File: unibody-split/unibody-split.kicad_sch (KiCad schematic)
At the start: 94 parts, among them IC1 AP130-20, SW1 SW_Push, SW10 SW_Push, SW11 SW_Push, SW12 SW_Push, SW13 SW_Push, SW14 SW_Push, SW15 SW_Push, SW16 SW_Push, SW17 SW_Push, SW18 SW_Push, SW19 SW_Push, SW2 SW_Push, SW20 SW_Push, SW21 SW_Push, SW22 SW_Push, SW23 SW_Push, SW24 SW_Push, SW25 SW_Push, SW26 SW_Push, SW27 SW_Push, SW28 SW_Push, SW29 SW_Push, SW3 SW_Push, SW30 SW_Push, SW31 SW_Push, SW32 SW_Push, SW33 SW_Push, SW34 SW_Push, SW35 SW_Push, SW36 SW_Push, SW37 SW_Push, SW38 SW_Push, SW39 SW_Push, SW4 SW_Push, SW40 SW_Push, SW41 SW_Push, SW42 SW_Push, SW5 SW_Push, SW6 SW_Push, SW7 SW_Push, SW8 SW_Push, SW9 SW_Push, U1 Pico, U2 PMW3360DM-T2QU, U3 HackPackv4-rescue:PSP_1000_JS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

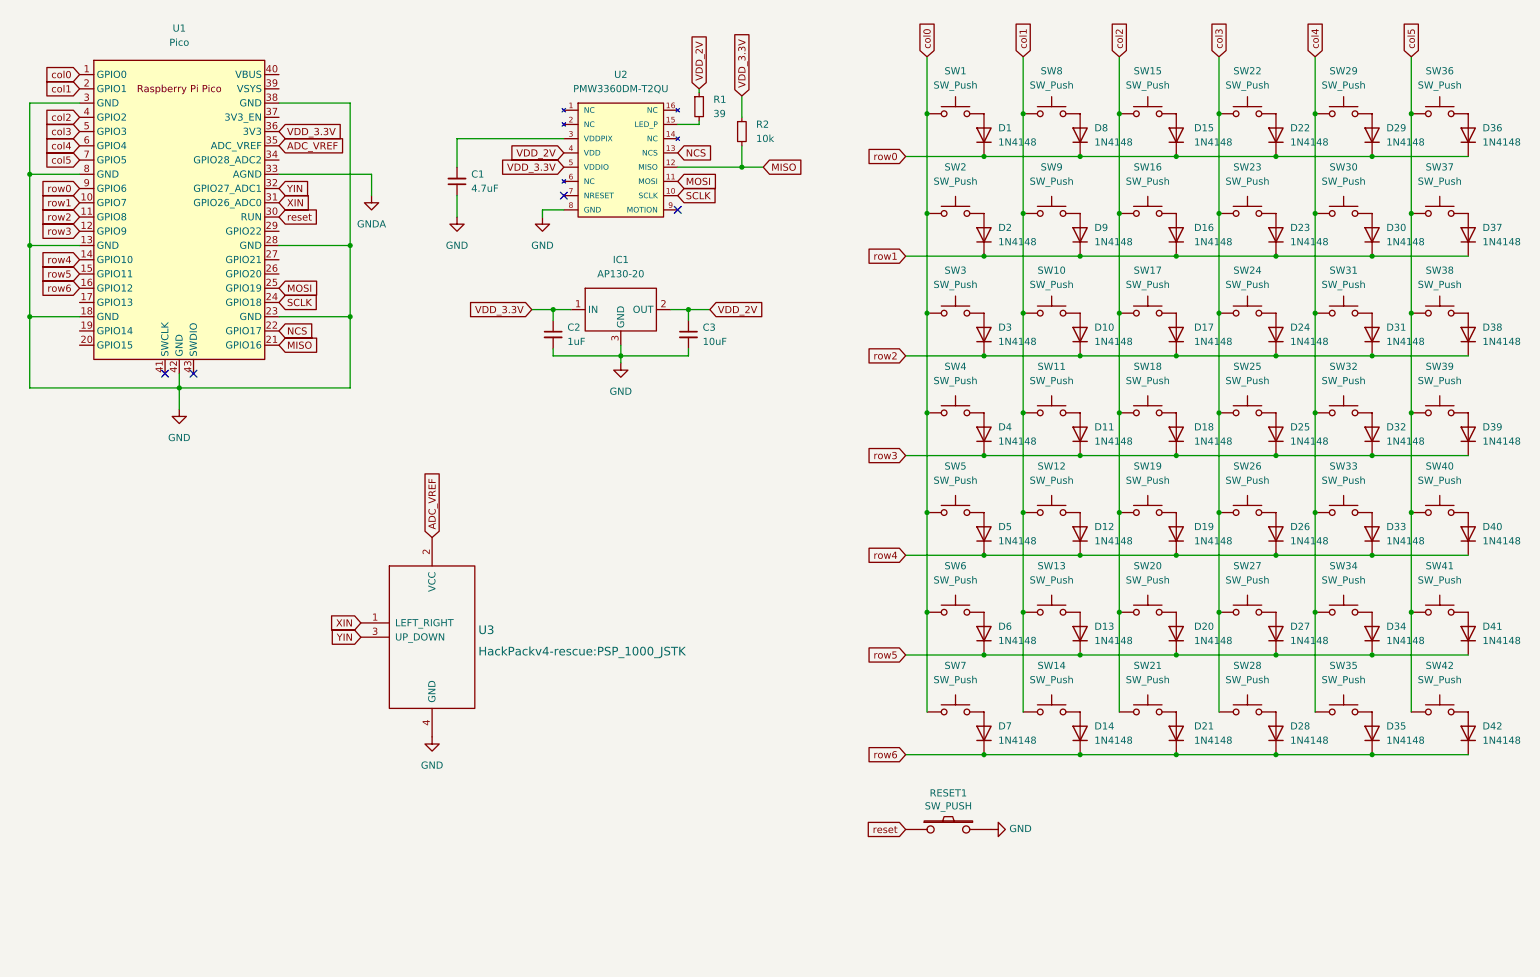
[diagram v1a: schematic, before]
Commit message: Add OLED to schematics
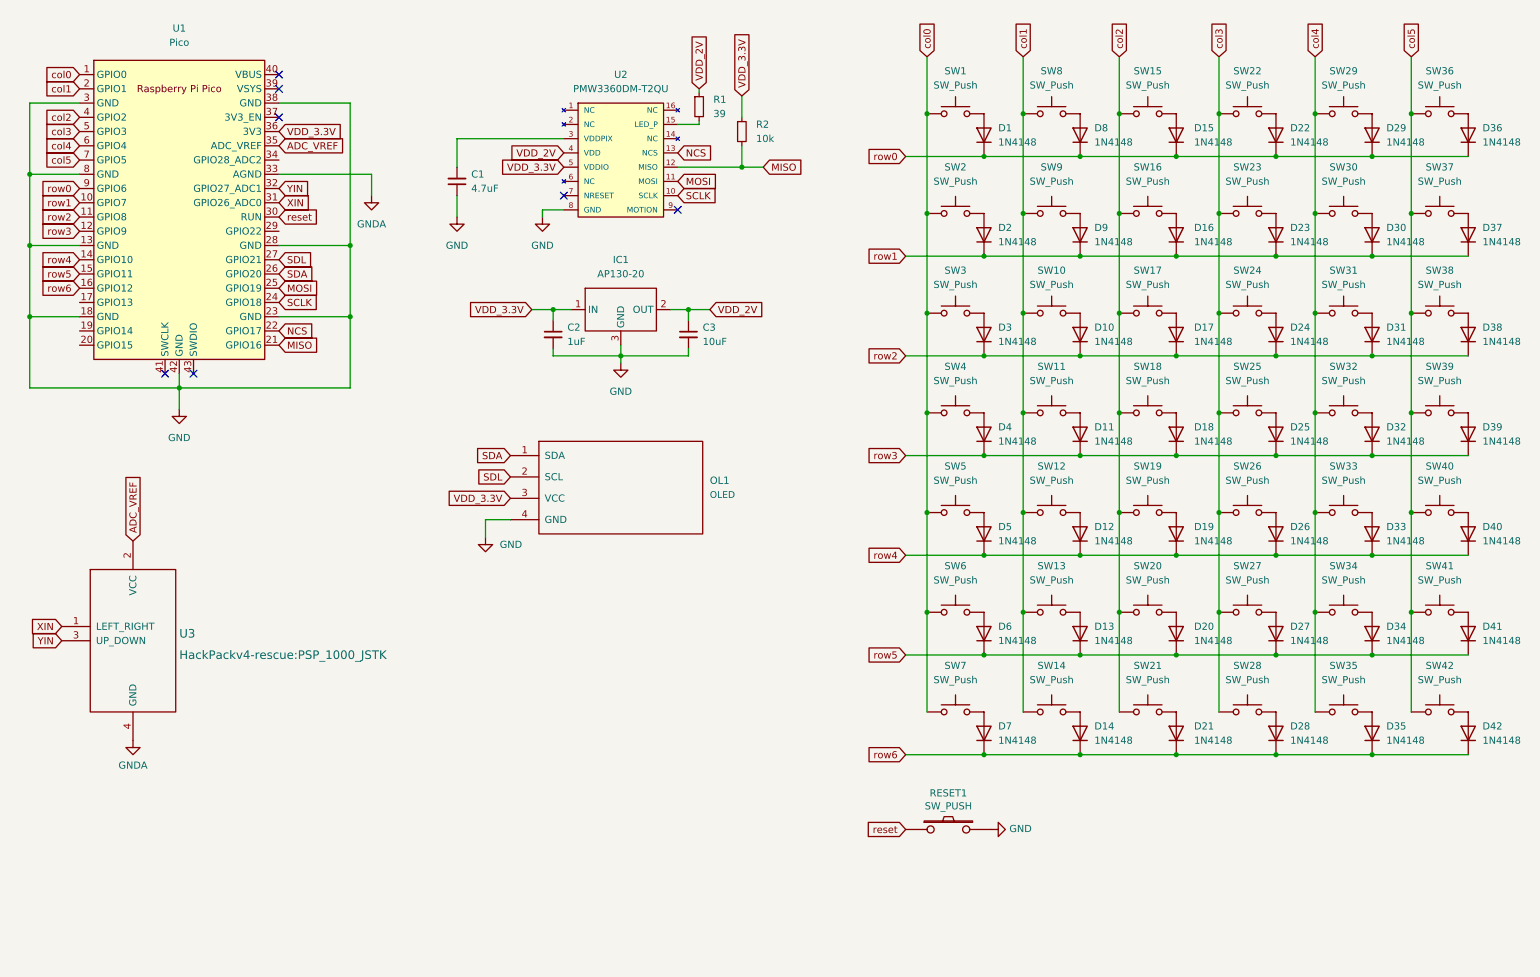
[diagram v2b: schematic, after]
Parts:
- added OL1: OLED, kbd:OLED_v2, symbol kbd:OLED
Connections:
- net GND: now also OL1.4 (GND); no longer U3.4 (GND)
- net GNDA: now also U3.4 (GND)
- net VDD_3.3V: now also OL1.3 (VCC)
- net SDA: now reaches U1.26 (GPIO20)
- net SDA: now also OL1.1 (SDA)
- net SDL: now reaches U1.27 (GPIO21)
- net SDL: now also OL1.2 (SCL)
- no-connect marks 4 -> 7
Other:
- moved on the sheet: U3
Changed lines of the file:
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@@
   (no_connect (at 111.76 45.72))
   (no_connect (at 132.08 48.26))
+  (no_connect (at 60.96 26.67))
+  (no_connect (at 60.96 31.75))
+  (no_connect (at 60.96 24.13))
   (no_connect (at 45.72 77.47))
   (no_connect (at 40.64 77.47))
@@
     (stroke (width 0) (type default) (color 0 0 0 0))
   )
+  (wire (pts (xy 102.235 103.505) (xy 97.79 103.505))
+    (stroke (width 0) (type default) (color 0 0 0 0))
+  )
   (wire (pts (xy 228.6 102.235) (xy 228.6 120.015))
     (stroke (width 0) (type default) (color 0 0 0 0))
@@
   )
   (wire (pts (xy 245.745 120.015) (xy 245.745 137.795))
+    (stroke (width 0) (type default) (color 0 0 0 0))
+  )
+  (wire (pts (xy 97.79 103.505) (xy 97.79 106.68))
     (stroke (width 0) (type default) (color 0 0 0 0))
   )
@@
     )
   )
+  (global_label "SDL" (shape input) (at 102.235 95.885 180) (fields_autoplaced)
+    (effects (font (size 1.27 1.27)) (justify right))
+    (property "Intersheet References" "${INTERSHEET_REFS}" (id 0) (at 96.3143 95.9644 0)
+      (effects (font (size 1.27 1.27)) (justify right) hide)
+    )
+  )
   (global_label "VDD_2V" (shape input) (at 135.89 26.67 90) (fields_autoplaced)
     (effects (font (size 1.27 1.27)) (justify left))
@@
     )
   )
+  (global_label "SDA" (shape input) (at 102.235 92.075 180) (fields_autoplaced)
+    (effects (font (size 1.27 1.27)) (justify right))
+    (property "Intersheet References" "${INTERSHEET_REFS}" (id 0) (at 96.2538 92.1544 0)
+      (effects (font (size 1.27 1.27)) (justify right) hide)
+    )
+  )
   (global_label "MOSI" (shape input) (at 132.08 43.18 0) (fields_autoplaced)
     (effects (font (size 1.27 1.27)) (justify left))
@@
     )
   )
+  (global_label "SDA" (shape input) (at 60.96 59.69 0) (fields_autoplaced)
+    (effects (font (size 1.27 1.27)) (justify left))
+    (property "Intersheet References" "${INTERSHEET_REFS}" (id 0) (at 66.9412 59.6106 0)
+      (effects (font (size 1.27 1.27)) (justify left) hide)
+    )
+  )
   (global_label "reset" (shape input) (at 172.72 158.75 180) (fields_autoplaced)
     (effects (font (size 1.27 1.27)) (justify right))
@@
     )
   )
-  (global_label "XIN" (shape input) (at 75.565 121.92 180) (fields_autoplaced)
-    (effects (font (size 1.27 1.27)) (justify right))
-    (property "Intersheet References" "${INTERSHEET_REFS}" (id 0) (at 70.0071 121.8406 0)
+  (global_label "XIN" (shape input) (at 22.225 122.555 180) (fields_autoplaced)
+    (effects (font (size 1.27 1.27)) (justify right))
+    (property "Intersheet References" "${INTERSHEET_REFS}" (id 0) (at 16.6671 122.4756 0)
       (effects (font (size 1.27 1.27)) (justify right) hide)
     )
@@
     )
   )
+  (global_label "VDD_3.3V" (shape input) (at 102.235 99.695 180) (fields_autoplaced)
+    (effects (font (size 1.27 1.27)) (justify right))
+    (property "Intersheet References" "${INTERSHEET_REFS}" (id 0) (at 91.1133 99.6156 0)
+      (effects (font (size 1.27 1.27)) (justify right) hide)
+    )
+  )
   (global_label "col4" (shape input) (at 245.745 20.955 90) (fields_autoplaced)
     (effects (font (size 1.27 1.27)) (justify left))
@@
     )
   )
-  (global_label "ADC_VREF" (shape input) (at 88.265 106.68 90) (fields_autoplaced)
+  (global_label "ADC_VREF" (shape input) (at 34.925 107.315 90) (fields_autoplaced)
     (effects (font (size 1.27 1.27)) (justify left))
-    (property "Intersheet References" "${INTERSHEET_REFS}" (id 0) (at 88.1856 95.0745 90)
+    (property "Intersheet References" "${INTERSHEET_REFS}" (id 0) (at 34.8456 95.7095 90)
       (effects (font (size 1.27 1.27)) (justify left) hide)
     )
@@
     )
   )
-  (global_label "YIN" (shape input) (at 75.565 124.46 180) (fields_autoplaced)
-    (effects (font (size 1.27 1.27)) (justify right))
-    (property "Intersheet References" "${INTERSHEET_REFS}" (id 0) (at 70.1281 124.3806 0)
+  (global_label "YIN" (shape input) (at 22.225 125.095 180) (fields_autoplaced)
+    (effects (font (size 1.27 1.27)) (justify right))
+    (property "Intersheet References" "${INTERSHEET_REFS}" (id 0) (at 16.7881 125.0156 0)
       (effects (font (size 1.27 1.27)) (justify right) hide)
     )
@@
     )
   )
+  (global_label "SDL" (shape input) (at 60.96 57.15 0) (fields_autoplaced)
+    (effects (font (size 1.27 1.27)) (justify left))
+    (property "Intersheet References" "${INTERSHEET_REFS}" (id 0) (at 66.8807 57.0706 0)
+      (effects (font (size 1.27 1.27)) (justify left) hide)
+    )
+  )
   (global_label "SCLK" (shape input) (at 60.96 64.77 0) (fields_autoplaced)
     (effects (font (size 1.27 1.27)) (justify left))
@@
     (pin "2")
   )
-  (symbol (lib_id "HackPackv4-cache:HackPackv4-rescue{colon}PSP_1000_JSTK") (at 88.265 123.19 0) (unit 1)
-    (in_bom yes) (on_board yes) (fields_autoplaced)
-    (property "Reference" "U3" (id 0) (at 96.52 123.19 0)
+  (symbol (lib_id "HackPackv4-cache:HackPackv4-rescue{colon}PSP_1000_JSTK") (at 34.925 123.825 0) (unit 1)
+    (in_bom yes) (on_board yes) (fields_autoplaced)
+    (property "Reference" "U3" (id 0) (at 43.18 123.825 0)
       (effects (font (size 1.524 1.524)) (justify left))
     )
-    (property "Value" "HackPackv4-rescue:PSP_1000_JSTK" (id 1) (at 96.52 127 0)
+    (property "Value" "HackPackv4-rescue:PSP_1000_JSTK" (id 1) (at 43.18 127.635 0)
       (effects (font (size 1.524 1.524)) (justify left))
     )
-    (property "Footprint" "HackPack_Footprints:JOYSTICK-PSP1000" (id 2) (at 121.285 140.97 0)
+    (property "Footprint" "HackPack_Footprints:JOYSTICK-PSP1000" (id 2) (at 67.945 141.605 0)
       (effects (font (size 1.524 1.524)) hide)
     )
-    (property "Datasheet" "" (id 3) (at 121.285 140.97 0)
+    (property "Datasheet" "" (id 3) (at 67.945 141.605 0)
       (effects (font (size 1.524 1.524)) hide)
     )
@@
     (pin "2")
   )
-  (symbol (lib_id "power:GND") (at 88.265 142.24 0) (unit 1)
-    (in_bom yes) (on_board yes) (fields_autoplaced)
-    (property "Reference" "#PWR06" (id 0) (at 88.265 148.59 0)
-      (effects (font (size 1.27 1.27)) hide)
-    )
-    (property "Value" "GND" (id 1) (at 88.265 147.32 0))
-    (property "Footprint" "" (id 2) (at 88.265 142.24 0)
-      (effects (font (size 1.27 1.27)) hide)
-    )
-    (property "Datasheet" "" (id 3) (at 88.265 142.24 0)
-      (effects (font (size 1.27 1.27)) hide)
-    )
-    (pin "1")
-  )
   (symbol (lib_id "Diode:1N4148") (at 220.98 88.265 90) (unit 1)
     (in_bom yes) (on_board yes) (fields_autoplaced)
@@
     (pin "1")
     (pin "2")
+  )
+  (symbol (lib_id "power:GNDA") (at 34.925 142.875 0) (unit 1)
+    (in_bom yes) (on_board yes) (fields_autoplaced)
+    (property "Reference" "#PWR06" (id 0) (at 34.925 149.225 0)
+      (effects (font (size 1.27 1.27)) hide)
+    )
+    (property "Value" "GNDA" (id 1) (at 34.925 147.32 0))
+    (property "Footprint" "" (id 2) (at 34.925 142.875 0)
+      (effects (font (size 1.27 1.27)) hide)
+    )
+    (property "Datasheet" "" (id 3) (at 34.925 142.875 0)
+      (effects (font (size 1.27 1.27)) hide)
+    )
+    (pin "1")
   )
   (symbol (lib_id "Diode:1N4148") (at 273.05 52.705 90) (unit 1)
@@
     (pin "2")
   )
+  (symbol (lib_id "kbd:OLED") (at 121.285 98.425 0) (unit 1)
+    (in_bom yes) (on_board yes) (fields_autoplaced)
+    (property "Reference" "OL1" (id 0) (at 137.795 96.52 0)
+      (effects (font (size 1.2954 1.2954)) (justify left))
+    )
+    (property "Value" "OLED" (id 1) (at 137.795 99.06 0)
+      (effects (font (size 1.1938 1.1938)) (justify left))
+    )
+    (property "Footprint" "kbd:OLED_v2" (id 2) (at 121.285 95.885 0)
+      (effects (font (size 1.524 1.524)) hide)
+    )
+    (property "Datasheet" "" (id 3) (at 121.285 95.885 0)
+      (effects (font (size 1.524 1.524)) hide)
+    )
+    (pin "1")
+    (pin "2")
+    (pin "3")
+    (pin "4")
+  )
   (symbol (lib_id "Device:C_Small") (at 109.855 70.485 0) (unit 1)
     (in_bom yes) (on_board yes)
@@
     (pin "2")
   )
+  (symbol (lib_id "power:GND") (at 97.79 106.68 0) (unit 1)
+    (in_bom yes) (on_board yes) (fields_autoplaced)
+    (property "Reference" "#PWR08" (id 0) (at 97.79 113.03 0)
+      (effects (font (size 1.27 1.27)) hide)
+    )
+    (property "Value" "GND" (id 1) (at 100.33 107.9499 0)
+      (effects (font (size 1.27 1.27)) (justify left))
+    )
+    (property "Footprint" "" (id 2) (at 97.79 106.68 0)
+      (effects (font (size 1.27 1.27)) hide)
+    )
+    (property "Datasheet" "" (id 3) (at 97.79 106.68 0)
+      (effects (font (size 1.27 1.27)) hide)
+    )
+    (pin "1")
+  )
   (symbol (lib_id "Diode:1N4148") (at 238.76 52.705 90) (unit 1)
     (in_bom yes) (on_board yes)
@@
       (reference "#PWR05") (unit 1) (value "GND") (footprint "")
     )
-    (path "/6ee8ed8a-f9e3-49c8-9ed2-6cebe4a20089"
-      (reference "#PWR06") (unit 1) (value "GND") (footprint "")
+    (path "/7544d682-48f4-4d73-9a2f-c2cc972acfab"
+      (reference "#PWR06") (unit 1) (value "GNDA") (footprint "")
     )
     (path "/41d2141b-2555-41d1-9b61-56c4033530d3"
       (reference "#PWR07") (unit 1) (value "GND") (footprint "")
     )
+    (path "/fd35e1a1-1864-4884-8a82-3d9a96437f1c"
+      (reference "#PWR08") (unit 1) (value "GND") (footprint "")
+    )
     (path "/2c0aa1bc-b313-4c7e-9ec0-14de776e66ba"
       (reference "C1") (unit 1) (value "4.7uF") (footprint "Capacitor_SMD:C_0805_2012Metric")
@@
       (reference "IC1") (unit 1) (value "AP130-20") (footprint "Package_TO_SOT_SMD:SOT-23")
     )
+    (path "/a8e7698b-c7a7-47cb-a0b9-26cf74a23d1b"
+      (reference "OL1") (unit 1) (value "OLED") (footprint "kbd:OLED_v2")
+    )
     (path "/680a68fc-2ed0-45fc-8a97-39ab1f619573"

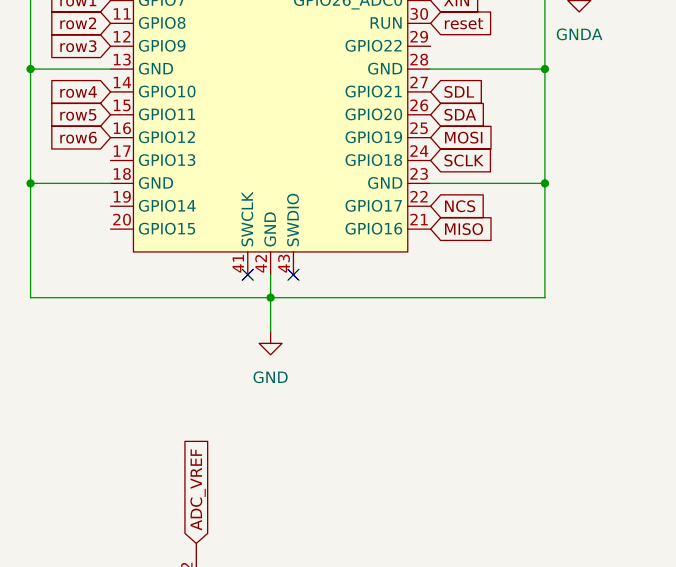
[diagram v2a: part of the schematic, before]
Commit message: disconnected bottom GND in RPi-Pico
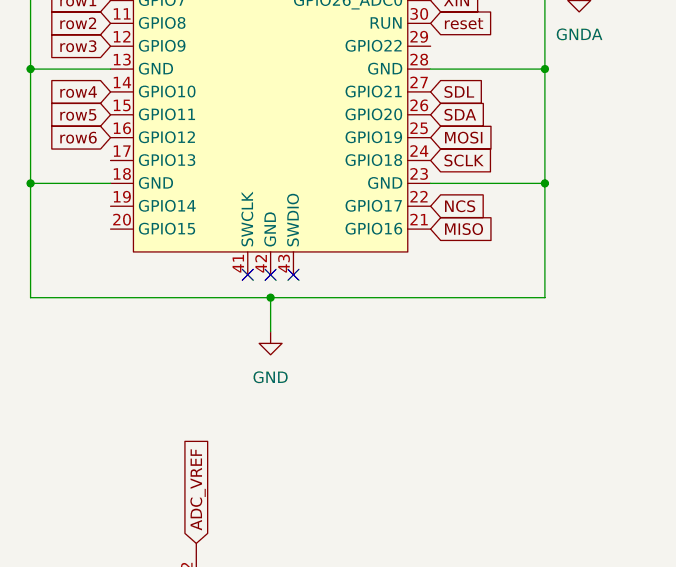
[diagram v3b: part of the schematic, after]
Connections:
- net GND: no longer U1.42 (GND)
- no-connect marks 7 -> 8
